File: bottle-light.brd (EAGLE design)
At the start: 88 x 88 mm, 55 parts, among them IC1 STM32F334K8T, IC2 LF33, X1 MINI-USB-SHIELD-UX60A-MB-5ST

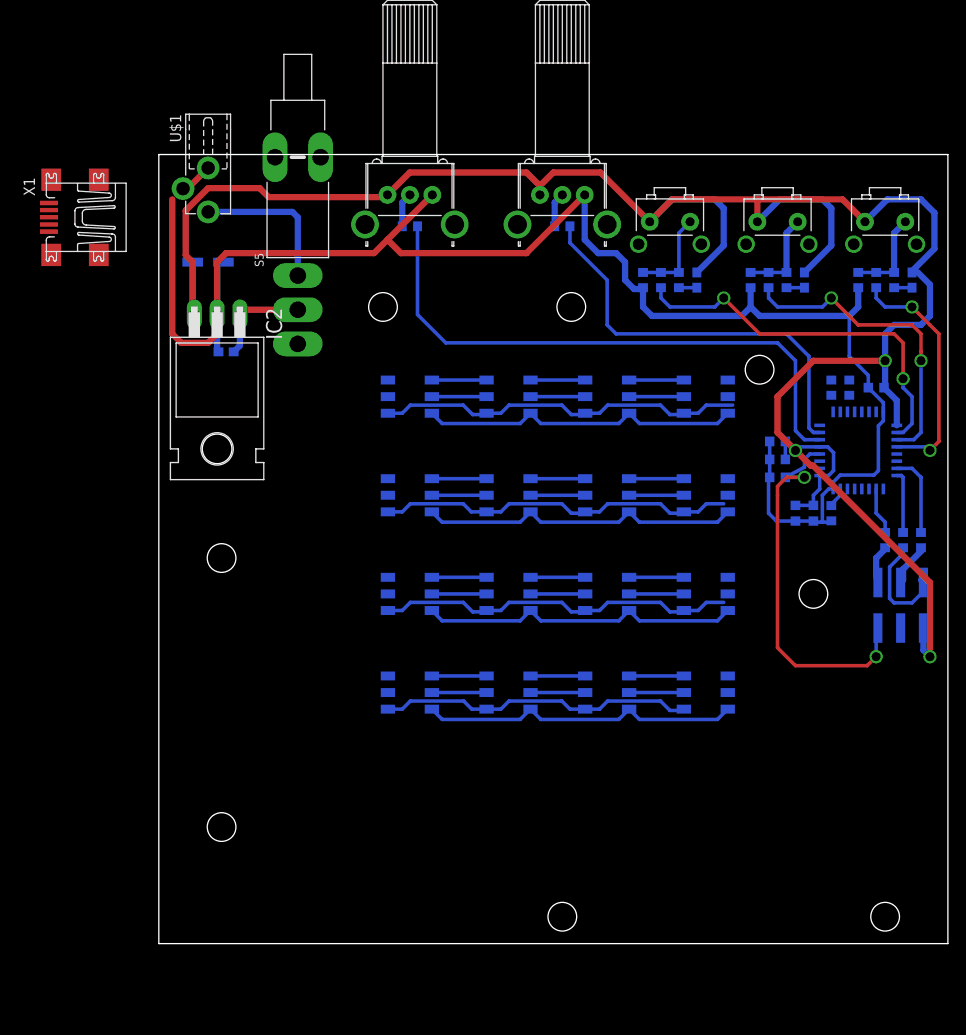
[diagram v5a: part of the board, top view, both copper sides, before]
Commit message: v0.2.2 LEDs connected and port for touch pad added
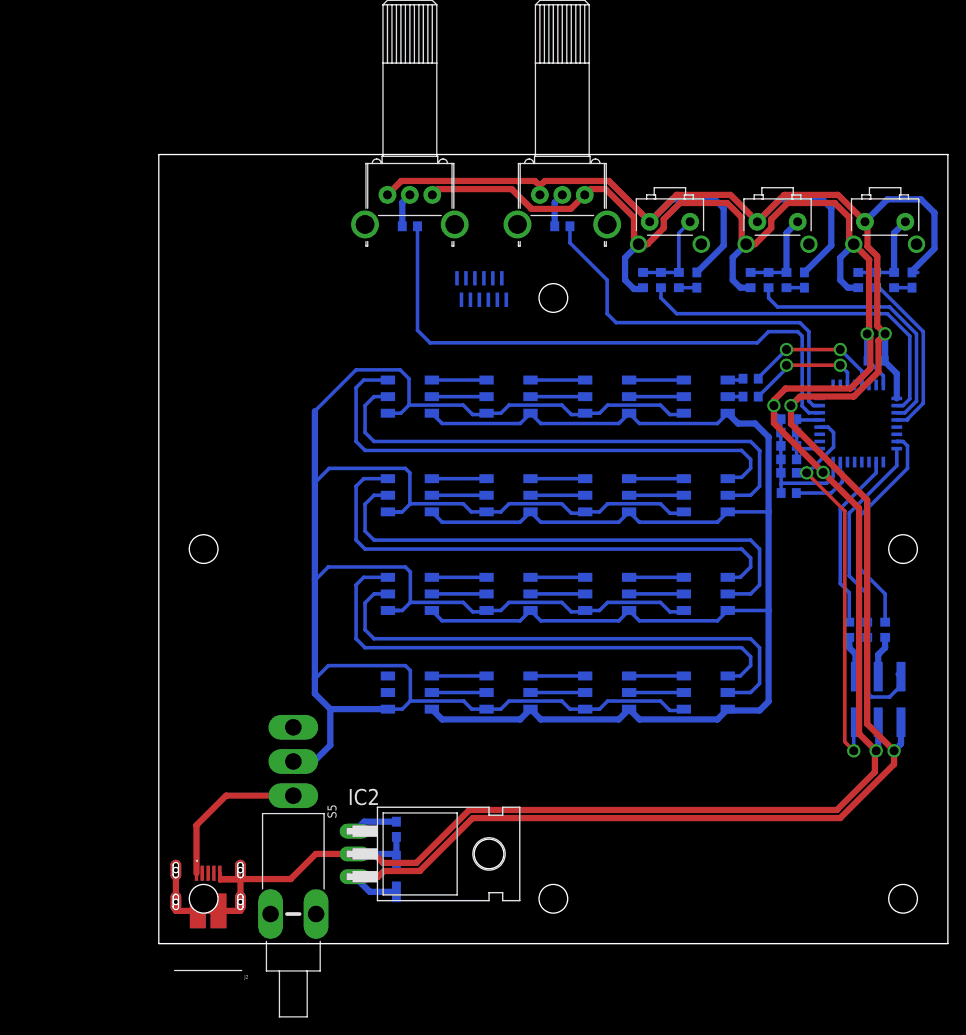
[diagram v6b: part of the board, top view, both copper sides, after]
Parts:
- removed U$1: BARREL_CONNECTOR_3.5MM, h8-conector:BARREL_CONNECTOR_3.5MM
- removed X1: MINI-USB-SHIELD-UX60A-MB-5ST, con-hirose:UX60A-MB-5ST
- added J1: 78127-1128, SamaSys:781271128
- added J2: UJ2-MIBH-4-SMT-TR, UJ2-MIBH-4-SMT-TR:CUIINC_UJ2-MIBH-4-SMT-TR
- moved C13 71.6 mm to (26.5, 7.50), turned to 270 degrees
- moved S5 58.0 mm to (15.0, 16.5), turned to 270 degrees
- moved C12 56.5 mm to (26.5, 12.8), turned to 270 degrees
- moved IC2 56.1 mm to (32.0, 10.0), turned to 270 degrees
- moved R2 11.0 mm to (66.0, 63.0), turned to 180 degrees
- moved JP1 10.8 mm to (81.5, 28.5)
- moved R20 10.8 mm to (81.0, 35.0)
- moved R21 10.8 mm to (79.0, 35.0)
- moved R22 10.8 mm to (77.0, 35.0)
- moved R1 9.06 mm to (66.0, 61.0), turned to 180 degrees
- moved C5 7.54 mm to (70.2, 55.5), turned to 0 degrees
- moved C2 6.60 mm to (70.2, 54.0), turned to 0 degrees
- moved R19 5.26 mm to (70.2, 50.2), turned to 180 degrees
- moved C4 3.25 mm to (70.2, 57.0)
- moved C3 3.00 mm to (80.0, 65.0)
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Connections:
- removed net N$76: S5.1, U$1.1
- new net 5V-IN: J2.1, S5.1
- net GND: now also J2.5, J2.P1, J2.P2, J2.P3, J2.P4, J2.P5, J2.P6; no longer U$1.2
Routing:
- net GND: track 331.2 -> 485.2 mm, vias 0 -> 10
- net +5V: track 168.7 -> 259.8 mm
- net N$52: track 0.00 -> 58.8 mm
- net N$61: track 0.00 -> 58.8 mm
- net N$60: track 0.00 -> 58.8 mm
- net N$53: track 0.00 -> 58.8 mm
- net N$45: track 0.00 -> 58.8 mm
- net N$44: track 0.00 -> 58.8 mm
- net +3V3: track 253.7 -> 283.9 mm
- net 5V-IN: track 0.00 -> 17.5 mm
- net N$76: track 16.7 -> 0.00 mm
- net N$1: track 6.93 -> 23.0 mm
- net N$24: track 9.26 -> 24.8 mm
- net N$3: track 0.00 -> 15.5 mm, vias 0 -> 2
- net N$25: track 5.26 -> 19.9 mm
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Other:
- board text added: "BottleLight v0.2.2 13.01.2019 cc-0 HansAchterbahn"

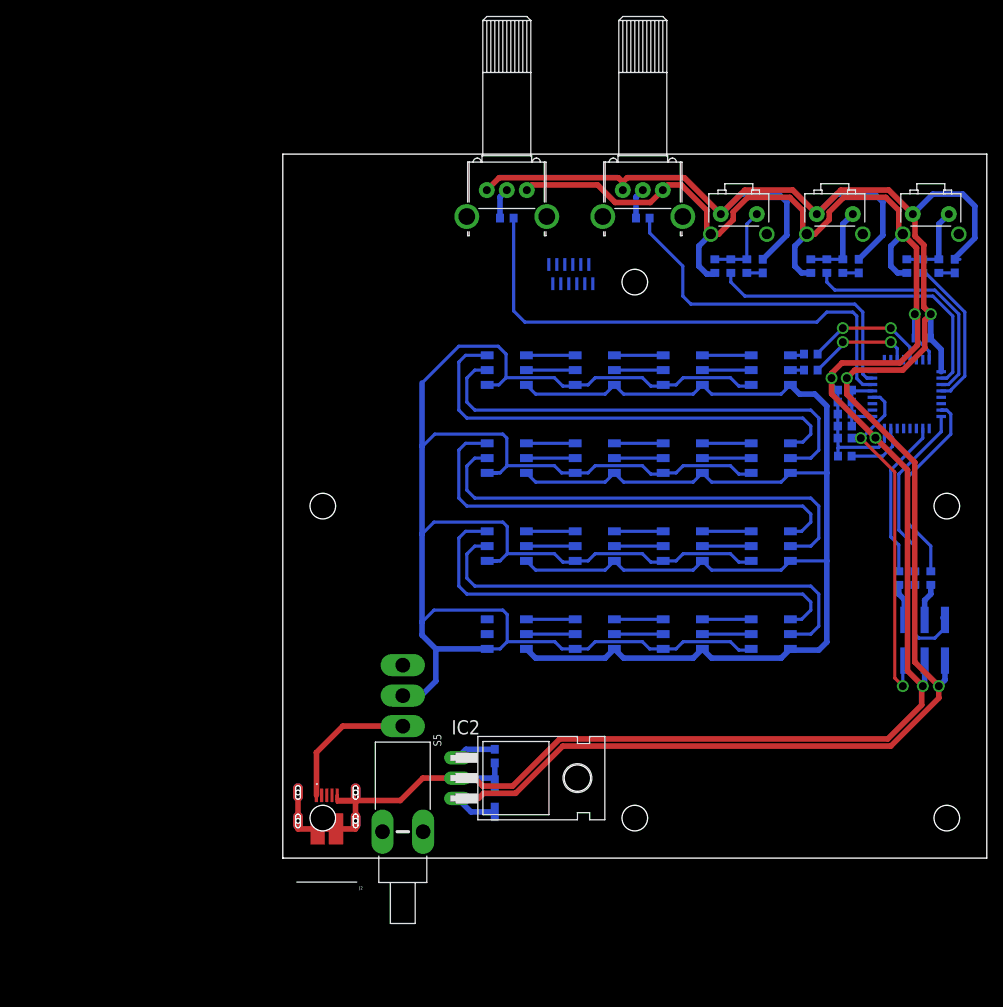
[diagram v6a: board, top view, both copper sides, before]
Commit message: v0.2.3 pinout and connection of touch pad to STM32 | changed library of buttons and potentiometers | added polygon on top and bottom| changed Micro-USB position
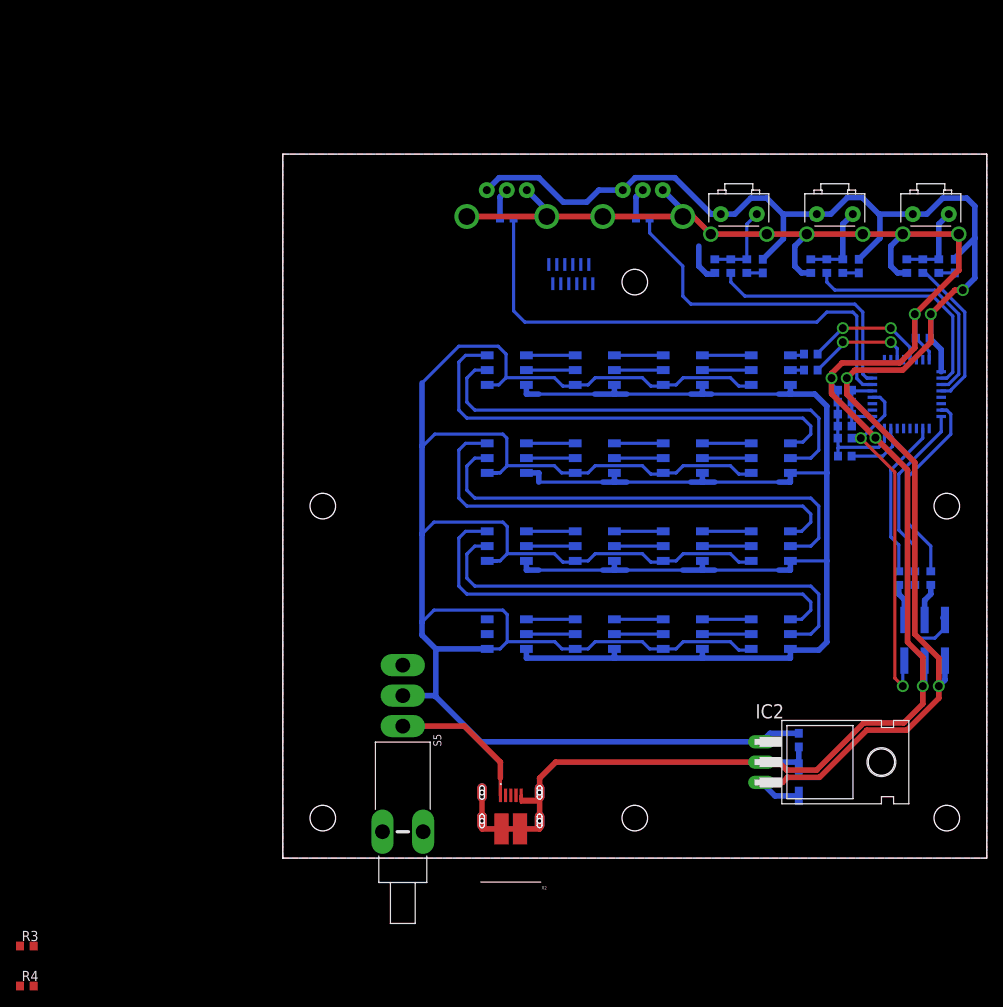
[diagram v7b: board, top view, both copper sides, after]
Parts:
- removed J2: UJ2-MIBH-4-SMT-TR, UJ2-MIBH-4-SMT-TR:CUIINC_UJ2-MIBH-4-SMT-TR
- added R3, R4: 8.2, resistor:R0603
- added X2: UJ2-MIBH-4-SMT-TR, UJ2-MIBH-4-SMT-TR:CUIINC_UJ2-MIBH-4-SMT-TR
- R25, R26: value RK09K -> 10k
- moved C12 38.1 mm to (64.5, 14.8)
- moved C13 38.1 mm to (64.5, 9.50)
- moved IC2 38.1 mm to (70.0, 12.0)
- renumbered J1 to X1, JP1 to X3
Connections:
- net POTI_COLOR renamed POTI-COLOR
- net POTI_LUMINOSITY renamed POTI-LUMINOSITY
- net SPI-CLK renamed LED-SPI-CLK
- new net !TOUCH-SPI-SS: X1.3
- new net LED-SPI-MOSI: R2.1
- new net N$4: IC1.29, R3.2
- new net N$5: IC1.30, R4.2
- new net TOUCH-BTN1: X1.8
- new net TOUCH-BTN2: X1.6
- new net TOUCH-BTN3: X1.7
- new net TOUCH-DR: X1.4
- new net TOUCH-I2C-SCL: R3.1, X1.9
- new net TOUCH-I2C-SDA: R4.1, X1.10
- new net TOUCH-SPI-MISO: X1.2
- new net TOUCH-SPI-MOSI: X1.5
- new net TOUCH-SPI-SCK: X1.1
- net +3V3: now also X1.12
- net 5V-IN: now also X2.1; no longer J2.1
- net GND: now also R25.NC1, R25.NC2, R26.NC1, R26.NC2, S2.NC1, S2.NC2, S3.NC1, S3.NC2, S4.NC1, S4.NC2, X1.11, X2.5, X2.P1, X2.P2, X2.P3, X2.P4, X2.P5, X2.P6; no longer J2.5, J2.P1, J2.P2, J2.P3, J2.P4, J2.P5, J2.P6
- net SPI-MOSI: no longer R2.1
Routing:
- net +3V3: track 283.9 -> 220.5 mm, vias 3 -> 4
- net +5V: track 259.8 -> 306.4 mm
- net GND: track 485.2 -> 476.1 mm, vias 10 -> 4
- net 5V-IN: track 17.5 -> 18.2 mm
- added copper zone on layer 1, net GND
- added copper zone on layer 16, net GND
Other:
- board text added: "BottleLight v0.2.3 09.06.2019 cc-0 HansAchterbahn"
- board text removed: "BottleLight v0.2.2 13.01.2019 cc-0 HansAchterbahn"

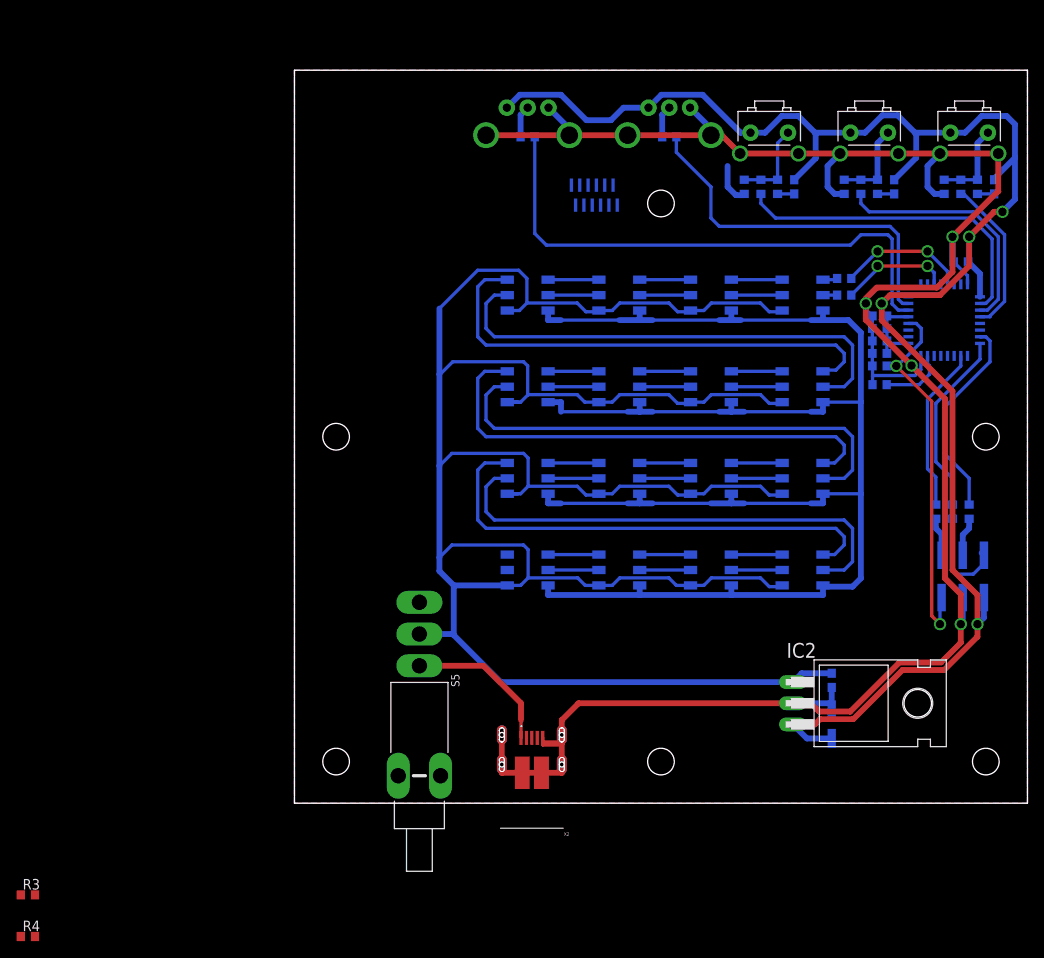
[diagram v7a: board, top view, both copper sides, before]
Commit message: v0.2.4 Device of Micro-USB  connector was defect -> repaired | removed buttons and color potentiometer | added incremental encoder | connected touch pad connector to I2C of STM32 | added MIT license | added a connector for connecting an optional APA102 Strip
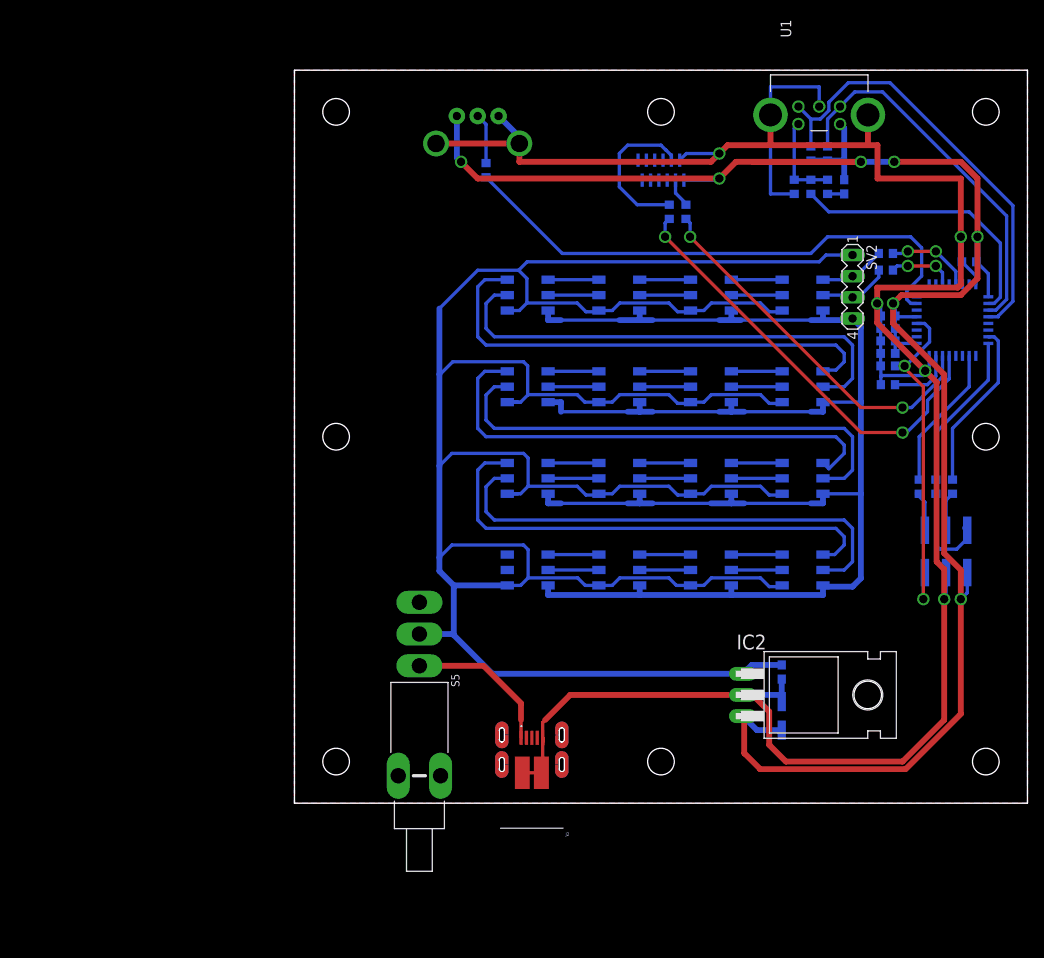
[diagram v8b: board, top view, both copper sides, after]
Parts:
- removed C8, C9: 100n, resistor:C0603
- removed R25: 10k, h8-rlc:RK09K
- removed R29: 8.2, resistor:R0603
- removed R33, R36: 100R, rcl:R0603
- removed R34, R37: 100k, rcl:R0603
- removed R35, R38: 330R, rcl:R0603
- removed S2, S3, S4: ALPS-SKHH, h8-switch:ALPS-SKHH
- removed X2: UJ2-MIBH-4-SMT-TR, UJ2-MIBH-4-SMT-TR:CUIINC_UJ2-MIBH-4-SMT-TR
- added J2: UJ2-MIBH-4-SMT-TR, UJ2-MIBH-4-SMT-TR:CUIINC_UJ2-MIBH-4-SMT-TR-2
- added R6, R7: 3k3, rcl:R0603
- added SV2: (no value), con-lstb:MA04-1
- added U1: EC11B15242AZ, EC11B15242AZ:EC11B15242AZ
- moved R4 117.5 mm to (47.0, 71.0), flipped to the bottom, turned to 270 degrees
- moved R3 112.5 mm to (45.0, 71.0), flipped to the bottom, turned to 270 degrees
- moved R26 23.0 mm to (22.0, 82.5)
- moved R28 22.4 mm to (23.0, 76.0), turned to 270 degrees
- moved X1 8.54 mm to (44.0, 76.0)
- moved C12 6.08 mm to (58.5, 15.8)
- moved C13 6.08 mm to (58.5, 10.5)
- moved IC2 6.08 mm to (64.0, 13.0)
- moved C7 6.00 mm to (66.0, 74.0)
- moved R30 6.00 mm to (64.0, 74.0)
- moved R31 6.00 mm to (60.0, 74.0)
- moved R32 6.00 mm to (62.0, 74.0)
- moved R1 5.83 mm to (71.0, 64.0)
- moved R2 5.83 mm to (71.0, 66.0)
- moved R20 3.61 mm to (79.0, 38.0)
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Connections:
- net USER-BUTTON1 renamed ENCODER-BUTTON
- removed net N$29: IC1.6, R29.2
- removed net N$32: R33.1, R34.2, R35.2, S3.1
- removed net N$33: C8.2, R33.2
- removed net N$35: R36.1, R37.2, R38.2, S4.1
- removed net N$36: C9.2, R36.2
- removed net POTI-COLOR: R25.2, R29.1
- removed net SPI-MOSI: LD1.1
- removed net USER-BUTTON2: IC1.19, R35.1
- removed net USER-BUTTON3: IC1.20, R38.1
- new net ENCODER-A: IC1.19, R7.2, U1.1
- new net ENCODER-B: IC1.20, R6.2, U1.2
- net +3V3: now also R6.1, R7.1, U1.4; no longer C8.1, C9.1, R25.3, S2.2, S3.2, S4.2
- net +5V: now also SV2.1
- net 5V-IN: now also J2.1; no longer X2.1
- net GND: now also J2.5, J2.P5, J2.P6, SV2.4, U1.3, U1.MH1, U1.MH2; no longer R25.1, R25.NC1, R25.NC2, R34.1, R37.1, S2.NC1, S2.NC2, S3.NC1, S3.NC2, S4.NC1, S4.NC2, X2.5, X2.P1, X2.P2, X2.P3, X2.P4, X2.P5, X2.P6
- net LED-SPI-CLK: now also SV2.3
- net LED-SPI-MOSI: now also LD1.1, SV2.2
- net N$30: now also U1.5; no longer S2.1
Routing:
- net N$29: track 65.9 -> 0.00 mm
- net ENCODER-B: track 0.00 -> 53.4 mm
- net N$4: track 0.00 -> 52.4 mm, vias 0 -> 2
- net N$5: track 0.00 -> 45.2 mm, vias 0 -> 2
- net ENCODER-A: track 0.00 -> 45.0 mm
- net +5V: track 306.4 -> 340.8 mm
- net USER-BUTTON2: track 29.5 -> 0.00 mm
- net N$34: track 44.0 -> 65.8 mm
- net USER-BUTTON3: track 19.1 -> 0.00 mm
- net TOUCH-I2C-SCL: track 0.00 -> 18.6 mm
- net +3V3: track 220.5 -> 238.8 mm, vias 4 -> 7
- net GND: track 476.1 -> 491.4 mm, vias 4 -> 5
- net N$35: track 10.2 -> 0.00 mm
- net N$32: track 10.2 -> 0.00 mm
- net LED-SPI-MOSI: track 0.00 -> 8.00 mm
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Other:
- board text added: "BottleLight v0.2.4 10.06.2019 HansAchterbahn MIT Licence"
- board text added: "ToDo: ----- - Poti wechseln -> an Drehencoder Dimensionen anpassen - Einschalter gegen dezenteren Typ austauschen - TouchPad anbindung überprüfen - Positionen prüfen: Poti, Drehencoder, Anschalter, Micro-USB-Schnittstelle - VDDA Beschaltung überprüfen"
- board text removed: "BottleLight v0.2.3 09.06.2019 cc-0 HansAchterbahn"
